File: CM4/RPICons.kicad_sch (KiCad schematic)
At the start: 4 parts, among them U1 Compute_Module_4_Connectors

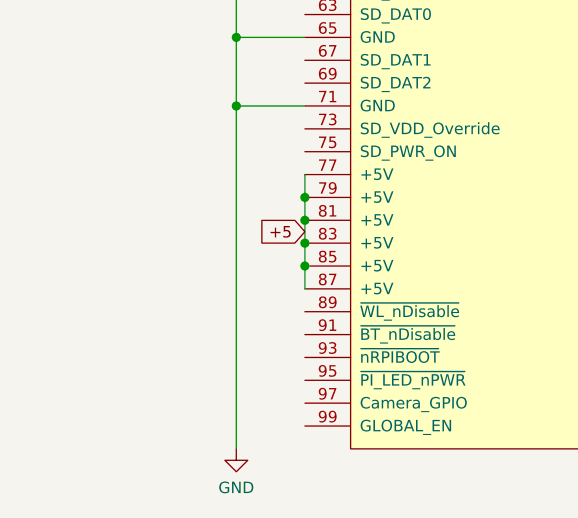
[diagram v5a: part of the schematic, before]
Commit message: added battery connecoectors and emmcbootdisable jumpper
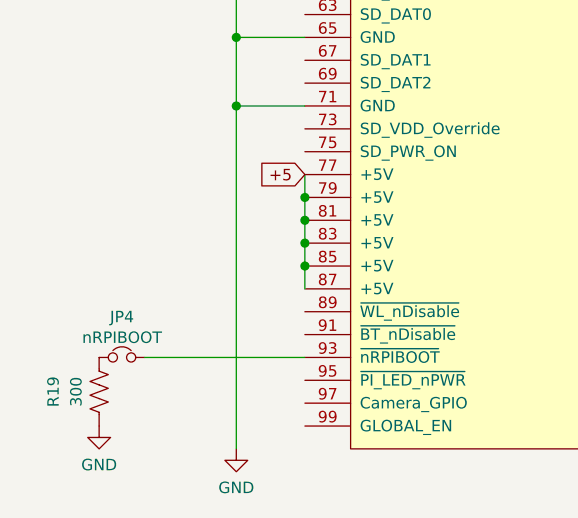
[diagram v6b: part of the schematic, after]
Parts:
- added JP4: nRPIBOOT, Connector_PinHeader_2.54mm:PinHeader_1x02_P2.54mm_Horizontal, symbol Device:Jumper_NC_Small
- added R19: 300, Resistor_SMD:R_1206_3216Metric, symbol Device:R_US
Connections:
- net GND: now also R19.1
- net at U1.93 (~nRPIBOOT): now also JP4.2
- new net: JP4.1, R19.2
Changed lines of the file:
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@@
+    (stroke (width 0) (type solid) (color 0 0 0 0))
+  )
+  (wire (pts (xy 33.655 149.86) (xy 51.435 149.86))
     (stroke (width 0) (type solid) (color 0 0 0 0))
   )
@@
     )
   )
-  (global_label "+5" (shape input) (at 51.435 135.89 180)
+  (global_label "+5" (shape input) (at 51.435 129.54 180)
     (effects (font (size 1.27 1.27)) (justify right))
-    (property "Intersheet References" "${INTERSHEET_REFS}" (id 0) (at 46.24 135.8106 0)
+    (property "Intersheet References" "${INTERSHEET_REFS}" (id 0) (at 46.24 129.4606 0)
       (effects (font (size 1.27 1.27)) (justify right) hide)
     )
@@
     (pin "1")
   )
+  (symbol (lib_id "power:GND") (at 28.575 157.48 0) (unit 1)
+    (in_bom yes) (on_board yes)
+    (property "Reference" "#PWR0147" (id 0) (at 28.575 163.83 0)
+      (effects (font (size 1.27 1.27)) hide)
+    )
+    (property "Value" "GND" (id 1) (at 28.575 161.8044 0))
+    (property "Footprint" "" (id 2) (at 28.575 157.48 0)
+      (effects (font (size 1.27 1.27)) hide)
+    )
+    (property "Datasheet" "" (id 3) (at 28.575 157.48 0)
+      (effects (font (size 1.27 1.27)) hide)
+    )
+    (pin "1")
+  )
   (symbol (lib_id "power:GND") (at 43.815 160.02 0) (unit 1)
     (in_bom yes) (on_board yes)
@@
     (pin "1")
   )
+  (symbol (lib_id "Device:Jumper_NC_Small") (at 31.115 149.86 0) (unit 1)
+    (in_bom yes) (on_board yes)
+    (property "Reference" "JP4" (id 0) (at 31.115 145.36 0))
+    (property "Value" "nRPIBOOT" (id 1) (at 31.115 147.6587 0))
+    (property "Footprint" "Connector_PinHeader_2.54mm:PinHeader_1x02_P2.54mm_Horizontal" (id 2) (at 31.115 149.86 0)
+      (effects (font (size 1.27 1.27)) hide)
+    )
+    (property "Datasheet" "~" (id 3) (at 31.115 149.86 0)
+      (effects (font (size 1.27 1.27)) hide)
+    )
+    (pin "1")
+    (pin "2")
+  )
+  (symbol (lib_id "Device:R_US") (at 28.575 153.67 180) (unit 1)
+    (in_bom yes) (on_board yes)
+    (property "Reference" "R19" (id 0) (at 23.495 153.67 90))
+    (property "Value" "300" (id 1) (at 26.035 153.67 90))
+    (property "Footprint" "Resistor_SMD:R_1206_3216Metric" (id 2) (at 27.559 153.416 90)
+      (effects (font (size 1.27 1.27)) hide)
+    )
+    (property "Datasheet" "~" (id 3) (at 28.575 153.67 0)
+      (effects (font (size 1.27 1.27)) hide)
+    )
+    (pin "1")
+    (pin "2")
+  )
   (symbol (lib_id "Device:R_US") (at 36.195 58.42 90) (unit 1)

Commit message: Finally Added the display!!!!
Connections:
- net piWatchDogPin: now also U1.40 (GPIO9); no longer U1.30 (GPIO6)
- net TP_SO: now reaches U1.28 (GPIO13)
- net LCD_SI/TP_SI: now reaches U1.31 (GPIO12)
- net LCD_RS: now reaches U1.34 (GPIO5)
- net TP_IRQ: now reaches U1.36 (ID_SD)
- net TP_CS: now reaches U1.38 (GPIO11)
- net LCD_CS: now reaches U1.44 (GPIO10)
- net SerialPin14 renamed LCD_SCK/TP_SCK
- new net RST: U1.30 (GPIO6)
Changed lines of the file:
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@@
     (stroke (width 0) (type solid) (color 0 0 0 0))
   )
+  (polyline (pts (xy 128.905 81.28) (xy 145.415 81.28))
+    (stroke (width 0) (type dash) (color 0 0 0 0))
+  )
   (text "PULL HIGH TO KEEP POWER ON\nPULL LOW TO POWER OFF 5V"
-    (at 130.048 70.358 0)
+    (at 146.558 83.693 0)
     (effects (font (size 1.27 1.27)) (justify left bottom))
   )
@@
     )
   )
+  (global_label "LCD_SCK{slash}TP_SCK" (shape input) (at 38.735 101.6 270)
+    (effects (font (size 1.27 1.27)) (justify right))
+    (property "Intersheet References" "${INTERSHEET_REFS}" (id 0) (at 38.6556 120.5836 90)
+      (effects (font (size 1.27 1.27)) (justify right) hide)
+    )
+  )
+  (global_label "LCD_SI{slash}TP_SI" (shape input) (at 51.435 71.12 180)
+    (effects (font (size 1.27 1.27)) (justify right))
+    (property "Intersheet References" "${INTERSHEET_REFS}" (id 0) (at 36.3219 71.0406 0)
+      (effects (font (size 1.27 1.27)) (justify right) hide)
+    )
+  )
   (global_label "+5" (shape input) (at 51.435 129.54 180)
     (effects (font (size 1.27 1.27)) (justify right))
@@
     )
   )
-  (global_label "piWatchDogPin" (shape input) (at 112.395 68.58 0)
+  (global_label "TP_SO" (shape input) (at 112.395 66.04 0)
     (effects (font (size 1.27 1.27)) (justify left))
-    (property "Intersheet References" "${INTERSHEET_REFS}" (id 0) (at 128.7176 68.6594 0)
+    (property "Intersheet References" "${INTERSHEET_REFS}" (id 0) (at 120.5533 65.9606 0)
       (effects (font (size 1.27 1.27)) (justify left) hide)
     )
+  )
+  (global_label "RST" (shape input) (at 112.395 68.58 0)
+    (effects (font (size 1.27 1.27)) (justify left))
+    (property "Intersheet References" "${INTERSHEET_REFS}" (id 0) (at 118.2552 68.5006 0)
+      (effects (font (size 1.27 1.27)) (justify left) hide)
+    )
+  )
+  (global_label "LCD_RS" (shape input) (at 112.395 73.66 0)
+    (effects (font (size 1.27 1.27)) (justify left))
+    (property "Intersheet References" "${INTERSHEET_REFS}" (id 0) (at 121.8233 73.5806 0)
+      (effects (font (size 1.27 1.27)) (justify left) hide)
+    )
+  )
+  (global_label "TP_IRQ" (shape input) (at 112.395 76.2 0)
+    (effects (font (size 1.27 1.27)) (justify left))
+    (property "Intersheet References" "${INTERSHEET_REFS}" (id 0) (at 121.2186 76.1206 0)
+      (effects (font (size 1.27 1.27)) (justify left) hide)
+    )
+  )
+  (global_label "TP_CS" (shape input) (at 112.395 78.74 0)
+    (effects (font (size 1.27 1.27)) (justify left))
+    (property "Intersheet References" "${INTERSHEET_REFS}" (id 0) (at 120.4929 78.6606 0)
+      (effects (font (size 1.27 1.27)) (justify left) hide)
+    )
+  )
+  (global_label "piWatchDogPin" (shape input) (at 112.395 81.28 0)
+    (effects (font (size 1.27 1.27)) (justify left))
+    (property "Intersheet References" "${INTERSHEET_REFS}" (id 0) (at 128.7176 81.3594 0)
+      (effects (font (size 1.27 1.27)) (justify left) hide)
+    )
+  )
+  (global_label "LCD_CS" (shape input) (at 112.395 86.36 0)
+    (effects (font (size 1.27 1.27)) (justify left))
+    (property "Intersheet References" "${INTERSHEET_REFS}" (id 0) (at 121.8233 86.2806 0)
+      (effects (font (size 1.27 1.27)) (justify left) hide)
+    )

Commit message: Started the "fun" of routing
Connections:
- net usbOTG_ID: now reaches TP12.1, U1.101 (USB_OTG_ID)
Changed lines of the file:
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@@
+    )
+  )
+  (global_label "usbOTG_ID" (shape input) (at 186.69 27.305 180)
+    (effects (font (size 1.27 1.27)) (justify right))
+    (property "Intersheet References" "${INTERSHEET_REFS}" (id 0) (at 174.5402 27.2256 0)
+      (effects (font (size 1.27 1.27)) (justify right) hide)
     )
   )
